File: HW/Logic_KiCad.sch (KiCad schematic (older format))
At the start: 10 parts

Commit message: add charger
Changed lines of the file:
@@
 	2300 6750 2500 6750
 $Sheet
-S 1100 4650 1100 500
+S 1850 5250 1100 500
 U 5F751135
 F0 "nabijecka.sch" 50
 F1 "nabijecka.sch" 50
+F2 "bat_+" I L 1850 5350 50
+F3 "bat_gnd" I L 1850 5500 50
 $EndSheet
+$Comp
+L power:GND #PWR?
+U 1 1 5F73DAEF
+P 1700 5500
+F 0 "#PWR?" H 1700 5250 50  0001 C CNN
+F 1 "GND" H 1705 5327 50  0000 C CNN
+F 2 "" H 1700 5500 50  0001 C CNN
+F 3 "" H 1700 5500 50  0001 C CNN
+	1    1700 5500
+	0    1    1    0
+$EndComp
+Wire Wire Line
+	1700 5500 1850 5500
+Text GLabel 1650 5350 0    50   Input ~ 0
+V_BAT_PRIME
+Wire Wire Line
+	1650 5350 1850 5350
 $EndSCHEMATC

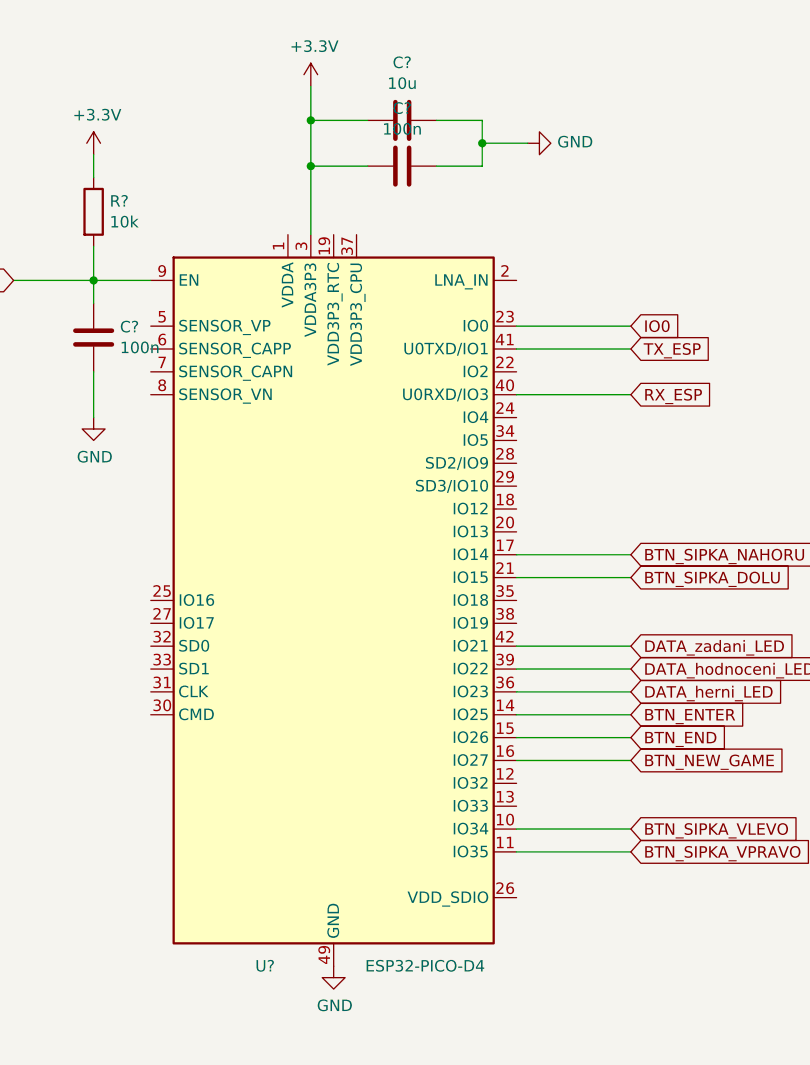
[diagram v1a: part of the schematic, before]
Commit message: add power supply for ESP, erase resistors by buttons, add power supply for CP2102, add communication control (CP2102-ESP)
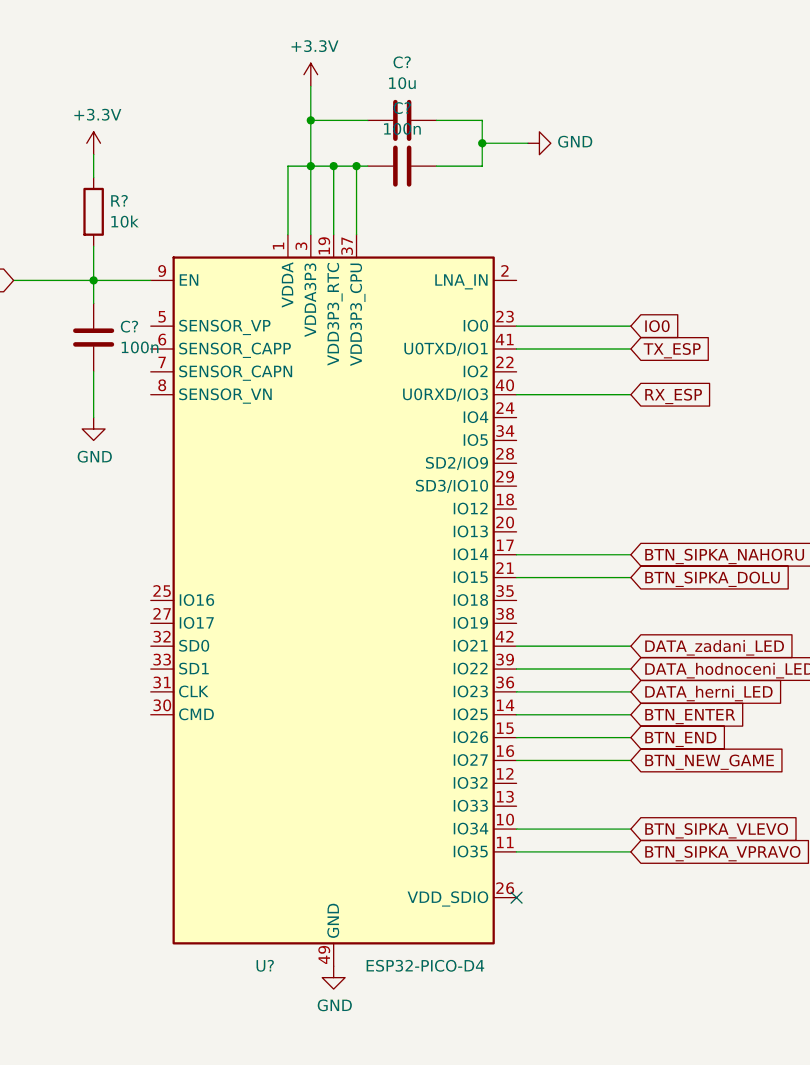
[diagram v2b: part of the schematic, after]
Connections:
- net +3V3: now also U?.1 (VDDA), U?.19 (VDD3P3_RTC), U?.37 (VDD3P3_CPU), U?.43 (VDDA), U?.46 (VDDA)
- no-connect marks 0 -> 1
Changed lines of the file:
@@
 $Descr A4 11693 8268
 encoding utf-8
-Sheet 1 9
+Sheet 1 16
 Title ""
 Date ""
@@
 	4800 1750 4800 1600
 Wire Wire Line
-	5050 1950 4800 1950
+	5050 1950 5000 1950
 Connection ~ 4800 1950
 Wire Wire Line
@@
 Wire Wire Line
 	1650 5350 1850 5350
+Wire Wire Line
+	4800 1950 4700 1950
+Wire Wire Line
+	4700 1950 4700 2250
+Wire Wire Line
+	4900 2250 4900 1950
+Connection ~ 4900 1950
+Wire Wire Line
+	4900 1950 4800 1950
+Wire Wire Line
+	5000 2250 5000 1950
+Connection ~ 5000 1950
+Wire Wire Line
+	5000 1950 4900 1950
+NoConn ~ 5700 5150
 $EndSCHEMATC

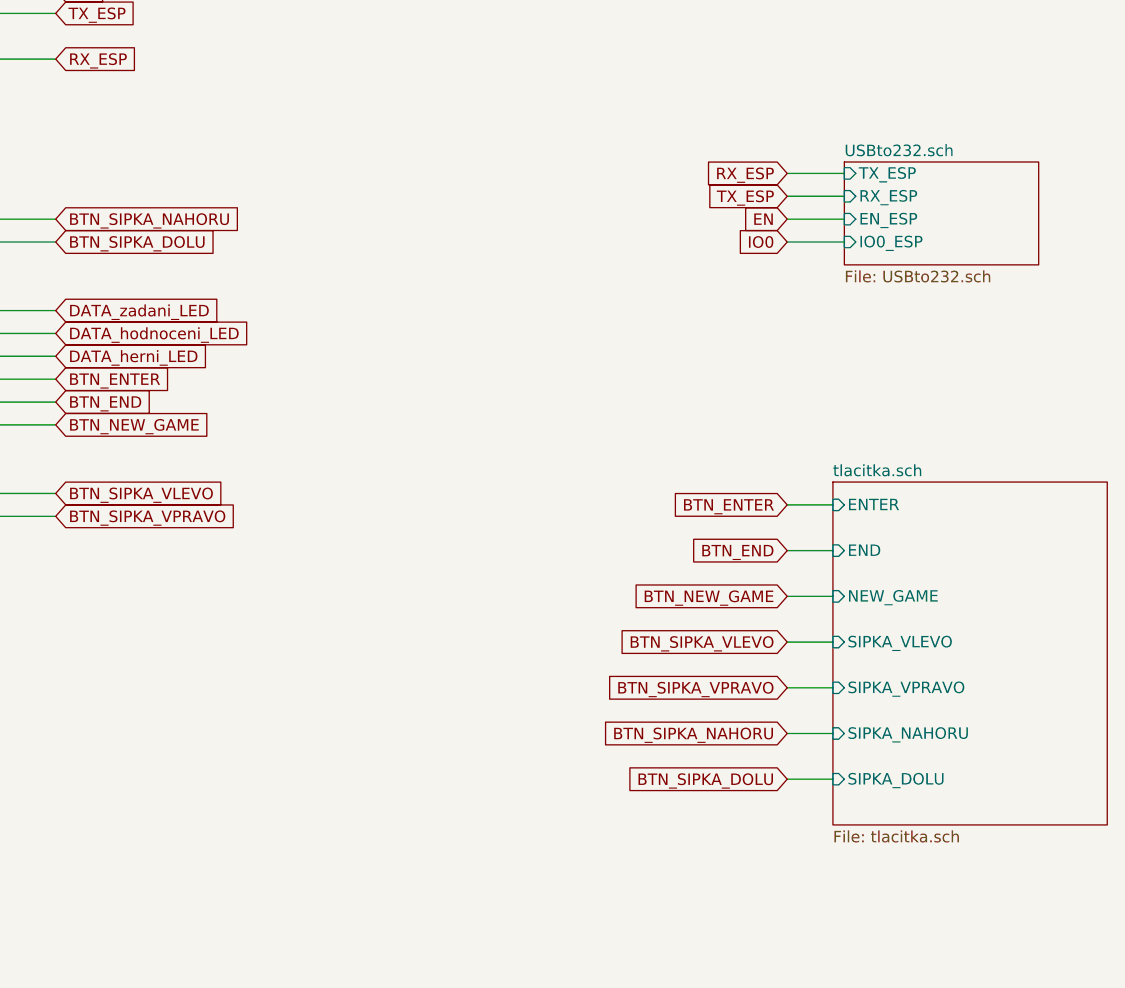
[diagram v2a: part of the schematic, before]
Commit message: change USB
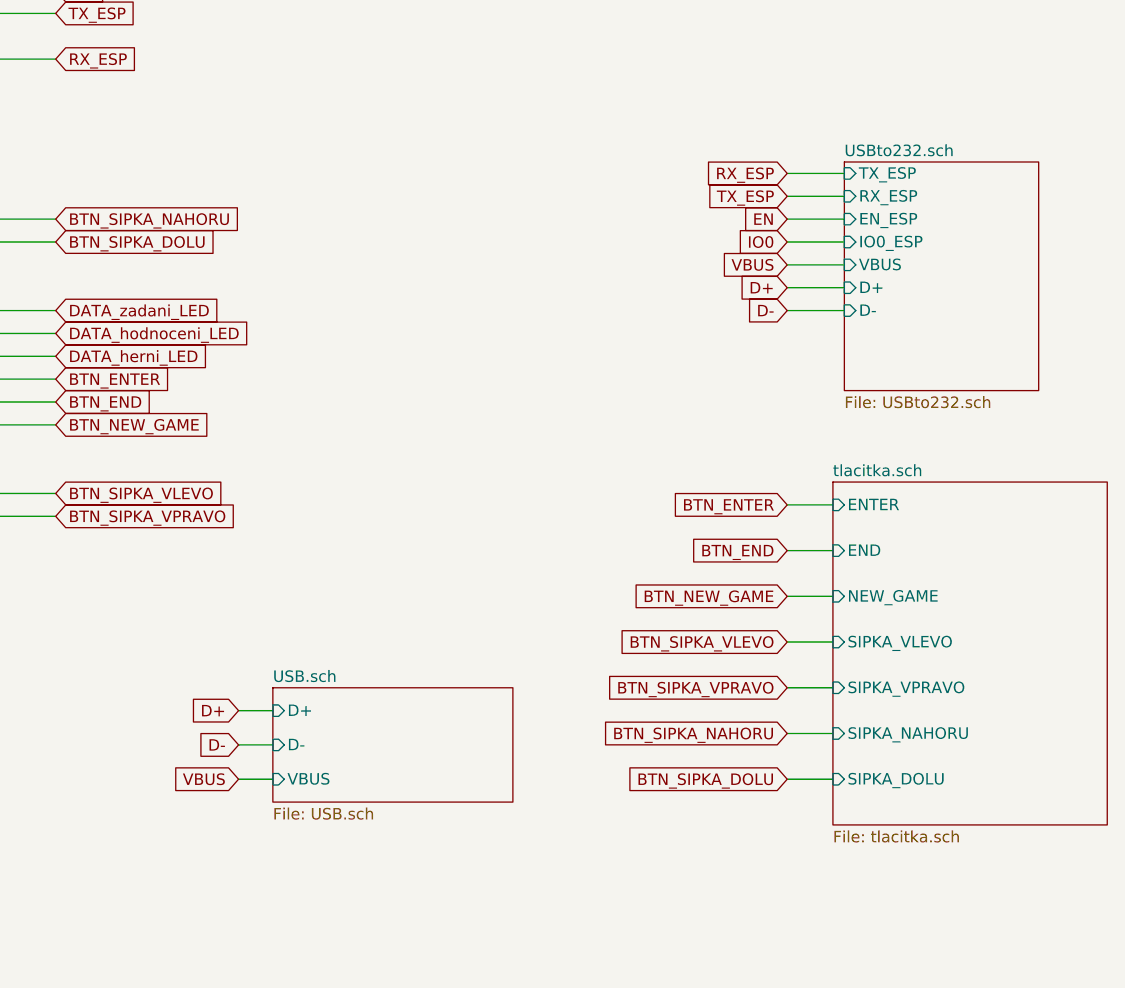
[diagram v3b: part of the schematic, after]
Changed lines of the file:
@@
 $Descr A4 11693 8268
 encoding utf-8
-Sheet 1 16
+Sheet 1 17
 Title ""
 Date ""
@@
 $EndSheet
 $Sheet
-S 9650 3400 850  450
+S 9650 3400 850  1000
 U 5FBB3550
 F0 "USBto232.sch" 50
@@
 F4 "EN_ESP" I L 9650 3650 50
 F5 "IO0_ESP" I L 9650 3750 50
+F6 "VBUS" I L 9650 3850 50
+F7 "D+" I L 9650 3950 50
+F8 "D-" I L 9650 4050 50
 $EndSheet
 Text GLabel 9400 3550 0    50   Input ~ 0
@@
 	5000 1950 4900 1950
 NoConn ~ 5700 5150
+$Sheet
+S 7150 5700 1050 500
+U 5F78DB3E
+F0 "USB.sch" 50
+F1 "USB.sch" 50
+F2 "D+" I L 7150 5800 50
+F3 "D-" I L 7150 5950 50
+F4 "VBUS" I L 7150 6100 50
+$EndSheet
+Text GLabel 9400 3850 0    50   Input ~ 0
+VBUS
+Text GLabel 9400 3950 0    50   Input ~ 0
+D+
+Text GLabel 9400 4050 0    50   Input ~ 0
+D-
+Wire Wire Line
+	9400 3850 9650 3850
+Wire Wire Line
+	9650 3950 9400 3950
+Wire Wire Line
+	9400 4050 9650 4050
+Text GLabel 7000 6100 0    50   Input ~ 0
+VBUS
+Text GLabel 7000 5800 0    50   Input ~ 0
+D+
+Text GLabel 7000 5950 0    50   Input ~ 0
+D-
+Wire Wire Line
+	7000 5800 7150 5800
+Wire Wire Line
+	7000 5950 7150 5950
+Wire Wire Line
+	7000 6100 7150 6100
 $EndSCHEMATC

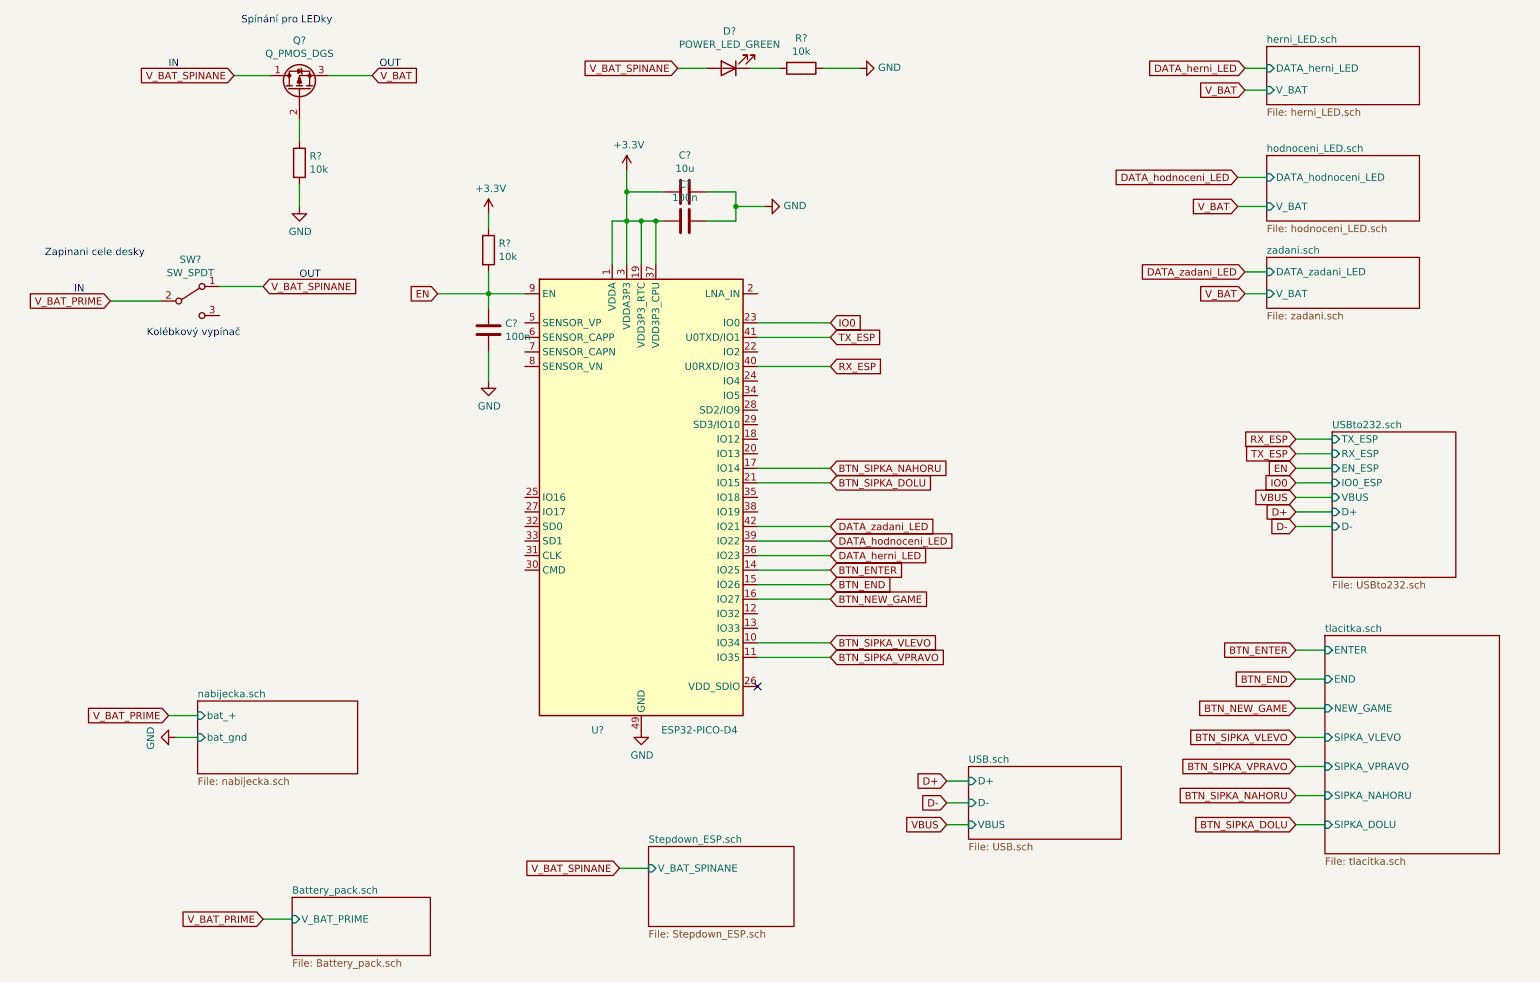
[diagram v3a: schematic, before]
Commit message: changed switching power supply for LEDs
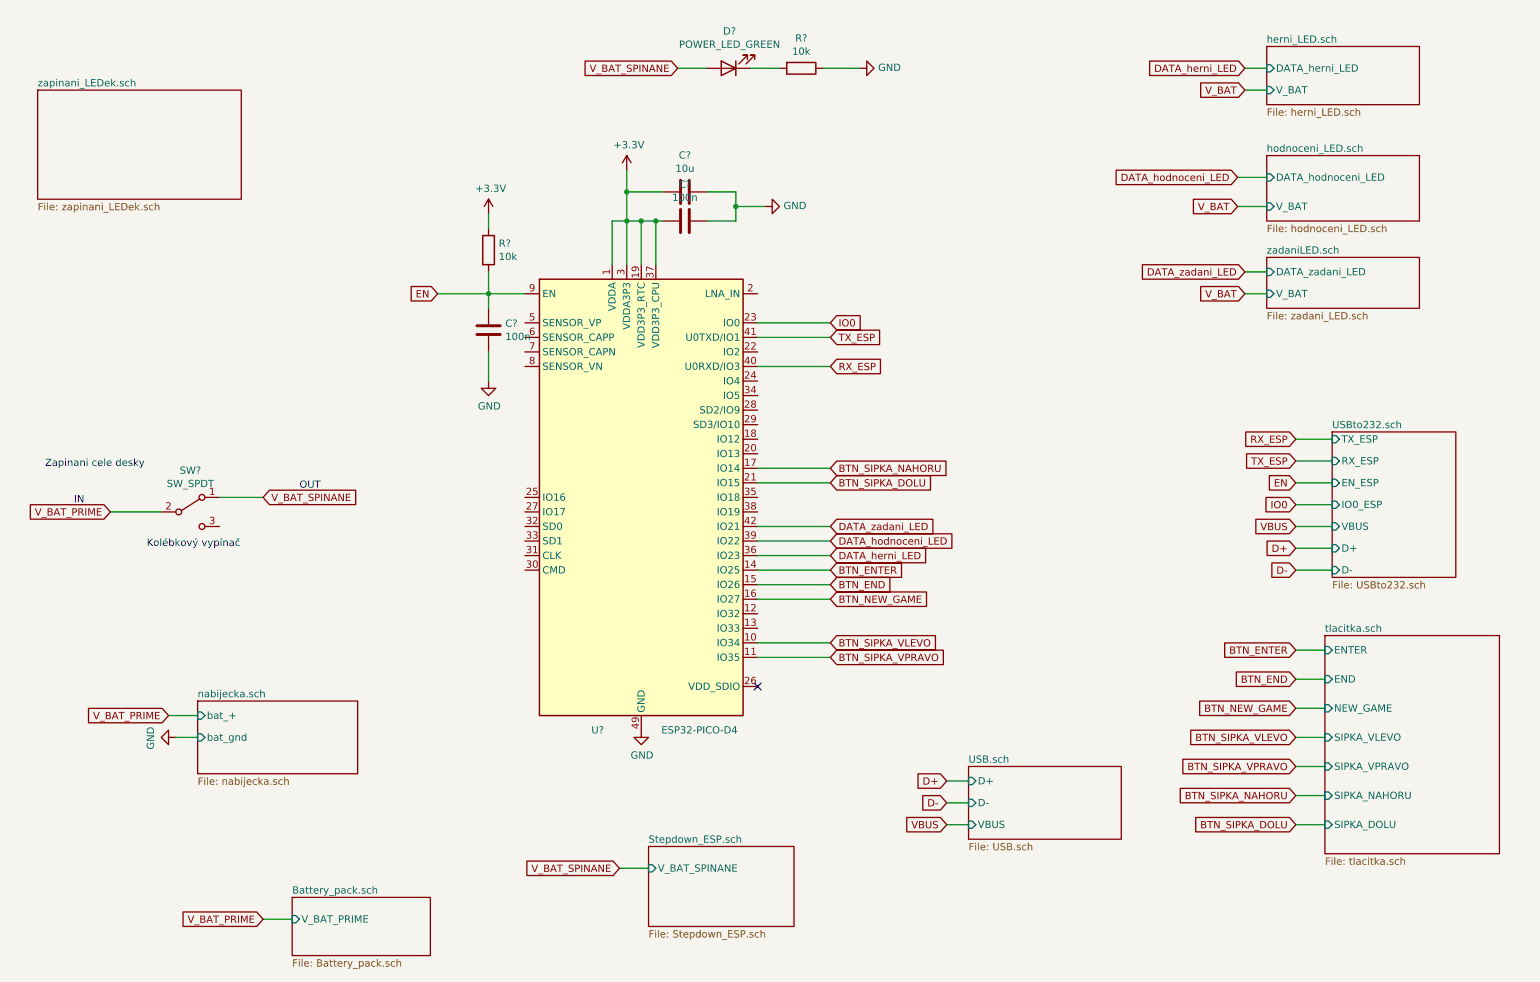
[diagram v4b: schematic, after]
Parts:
- removed Q?: Q_PMOS_DGS, symbol Device:Q_PMOS_DGS
- removed R?: 10k, Resistor_SMD:R_0402_1005Metric, symbol Device:R
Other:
- note removed: "Spínání pro LEDky"
- moved on the sheet: SW?
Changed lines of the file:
@@
 $Descr A4 11693 8268
 encoding utf-8
-Sheet 1 17
+Sheet 1 22
 Title ""
 Date ""
@@
 S 9200 2200 1050 350
 U 5FB682DC
-F0 "zadani.sch" 50
-F1 "zadani.sch" 50
+F0 "zadaniLED.sch" 50
+F1 "zadani_LED.sch" 50
 F2 "DATA_zadani_LED" I L 9200 2300 50
 F3 "V_BAT" I L 9200 2450 50
@@
 F1 "USBto232.sch" 50
 F2 "TX_ESP" I L 9650 3450 50
-F3 "RX_ESP" I L 9650 3550 50
-F4 "EN_ESP" I L 9650 3650 50
-F5 "IO0_ESP" I L 9650 3750 50
-F6 "VBUS" I L 9650 3850 50
-F7 "D+" I L 9650 3950 50
-F8 "D-" I L 9650 4050 50
-$EndSheet
-Text GLabel 9400 3550 0    50   Input ~ 0
+F3 "RX_ESP" I L 9650 3600 50
+F4 "EN_ESP" I L 9650 3750 50
+F5 "IO0_ESP" I L 9650 3900 50
+F6 "VBUS" I L 9650 4050 50
+F7 "D+" I L 9650 4200 50
+F8 "D-" I L 9650 4350 50
+$EndSheet
+Text GLabel 9400 3600 0    50   Input ~ 0
 TX_ESP
 Text GLabel 9400 3450 0    50   Input ~ 0
@@
 	9400 3450 9650 3450
 Wire Wire Line
-	9400 3550 9650 3550
-Text GLabel 9400 3650 0    50   Input ~ 0
+	9400 3600 9650 3600
+Text GLabel 9400 3750 0    50   Input ~ 0
 EN
-Text GLabel 9400 3750 0    50   Input ~ 0
+Text GLabel 9400 3900 0    50   Input ~ 0
 IO0
 Wire Wire Line
-	9400 3650 9650 3650
-Wire Wire Line
 	9400 3750 9650 3750
+Wire Wire Line
+	9400 3900 9650 3900
 $Comp
 L RF_Module:ESP32-PICO-D4 U?
@@
 Wire Wire Line
 	4750 6400 4950 6400
-$Comp
-L Device:Q_PMOS_DGS Q?
-U 1 1 5F71DB38
-P 2550 1050
-F 0 "Q?" V 2892 1050 50  0000 C CNN
-F 1 "Q_PMOS_DGS" V 2801 1050 50  0000 C CNN
-F 2 "" H 2750 1150 50  0001 C CNN
-F 3 "~" H 2550 1050 50  0001 C CNN
-	1    2550 1050
-	0    -1   -1   0
-$EndComp
-Text GLabel 2100 950  0    50   Input ~ 0
-V_BAT_SPINANE
-Text GLabel 3050 950  2    50   Input ~ 0
-V_BAT
-$Comp
-L power:GND #PWR?
-U 1 1 5F71E954
-P 2550 1850
-F 0 "#PWR?" H 2550 1600 50  0001 C CNN
-F 1 "GND" H 2555 1677 50  0000 C CNN
-F 2 "" H 2550 1850 50  0001 C CNN
-F 3 "" H 2550 1850 50  0001 C CNN
-	1    2550 1850
-	1    0    0    -1
-$EndComp
-$Comp
-L Device:R R?
-U 1 1 5F71EE20
-P 2550 1550
-F 0 "R?" H 2620 1596 50  0000 L CNN
-F 1 "10k" H 2620 1505 50  0000 L CNN
-F 2 "Resistor_SMD:R_0402_1005Metric" V 2480 1550 50  0001 C CNN
-F 3 "~" H 2550 1550 50  0001 C CNN
-	1    2550 1550
-	1    0    0    -1
-$EndComp
-Wire Wire Line
-	2100 950  2350 950
-Wire Wire Line
-	2750 950  3050 950
-Wire Wire Line
-	2550 1250 2550 1400
-Wire Wire Line
-	2550 1700 2550 1850
-Text Notes 2150 600  0    50   ~ 0
-Spínání pro LEDky
-Text GLabel 1250 2500 0    50   Input ~ 0
+Text GLabel 1250 3950 0    50   Input ~ 0
 V_BAT_PRIME
 $Comp
 L Switch:SW_SPDT SW?
 U 1 1 5F727A55
-P 1800 2500
-F 0 "SW?" H 1800 2785 50  0000 C CNN
-F 1 "SW_SPDT" H 1800 2694 50  0000 C CNN
-F 2 "" H 1800 2500 50  0001 C CNN
-F 3 "~" H 1800 2500 50  0001 C CNN
-	1    1800 2500
-	1    0    0    -1
-$EndComp
-Text GLabel 2300 2400 2    50   Input ~ 0
+P 1800 3950
+F 0 "SW?" H 1800 4235 50  0000 C CNN
+F 1 "SW_SPDT" H 1800 4144 50  0000 C CNN
+F 2 "" H 1800 3950 50  0001 C CNN
+F 3 "~" H 1800 3950 50  0001 C CNN
+	1    1800 3950
+	1    0    0    -1
+$EndComp
+Text GLabel 2300 3850 2    50   Input ~ 0
 V_BAT_SPINANE
 Wire Wire Line
-	2000 2400 2300 2400
-Wire Wire Line
-	1600 2500 1250 2500
-Text Notes 800  2200 0    50   ~ 0
+	2000 3850 2300 3850
+Wire Wire Line
+	1600 3950 1250 3950
+Text Notes 800  3650 0    50   ~ 0
 Zapinani cele desky\n
-Text Notes 1500 2750 0    50   ~ 0
+Text Notes 1500 4200 0    50   ~ 0
 Kolébkový vypínač
-Text Notes 1650 900  0    50   ~ 0
+Text Notes 1000 3900 0    50   ~ 0
 IN\n
-Text Notes 3100 900  0    50   ~ 0
-OUT\n
-Text Notes 1000 2450 0    50   ~ 0
-IN\n
-Text Notes 2550 2350 0    50   ~ 0
+Text Notes 2550 3800 0    50   ~ 0
 OUT\n
 Text GLabel 9400 4900 0    50   Input ~ 0
@@
 F4 "VBUS" I L 7150 6100 50
 $EndSheet
-Text GLabel 9400 3850 0    50   Input ~ 0
+Text GLabel 9400 4050 0    50   Input ~ 0
 VBUS
-Text GLabel 9400 3950 0    50   Input ~ 0
+Text GLabel 9400 4200 0    50   Input ~ 0
 D+
-Text GLabel 9400 4050 0    50   Input ~ 0
+Text GLabel 9400 4350 0    50   Input ~ 0
 D-
 Wire Wire Line
-	9400 3850 9650 3850
-Wire Wire Line
-	9650 3950 9400 3950
-Wire Wire Line
 	9400 4050 9650 4050
+Wire Wire Line
+	9650 4200 9400 4200
+Wire Wire Line
+	9400 4350 9650 4350
 Text GLabel 7000 6100 0    50   Input ~ 0
 VBUS
@@
 Wire Wire Line
 	7000 6100 7150 6100
+$Sheet
+S 750  1050 1400 750
+U 5F7BA54B
+F0 "zapinani_LEDek.sch" 50
+F1 "zapinani_LEDek.sch" 50
+$EndSheet
 $EndSCHEMATC
